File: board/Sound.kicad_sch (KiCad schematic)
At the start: 42 parts, among them J18 SJ1-3525N, J27 SND CT1/2, J39 LINE OUT, U57 YM2151, U58 YM3012, U59 TL074, U89 TDA2822M

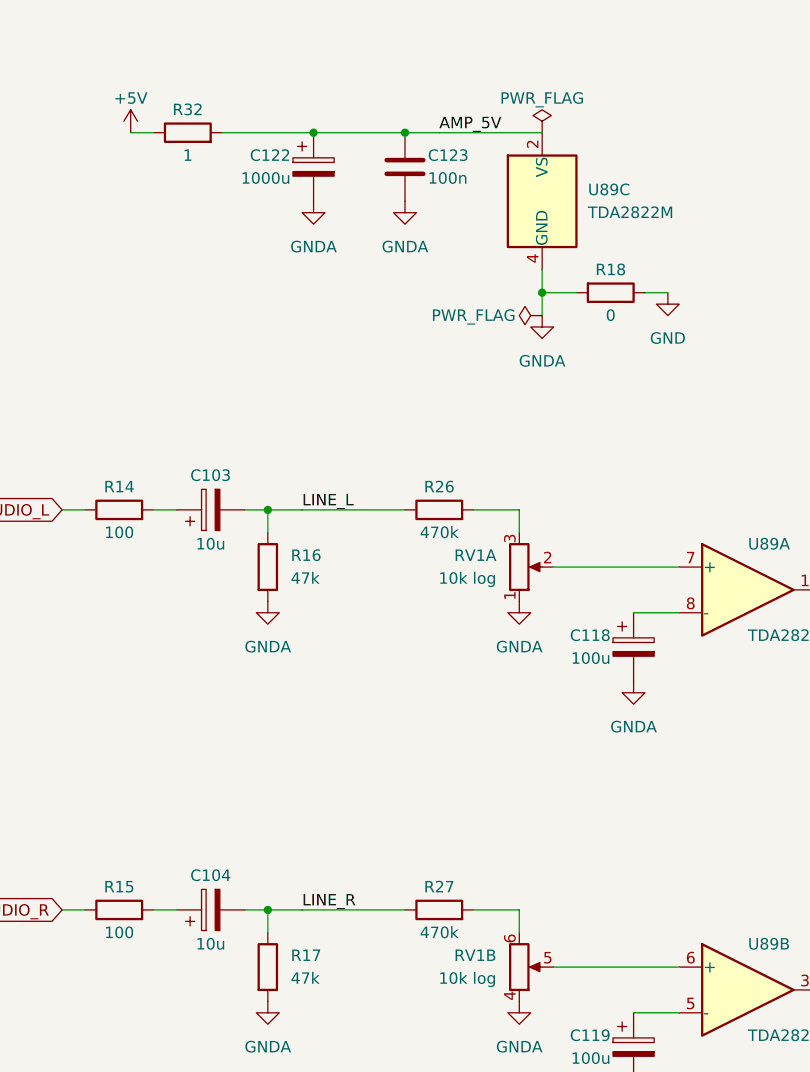
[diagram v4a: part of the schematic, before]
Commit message: V2.0: consolidate parts (239 -> 216), GAL C rev 02
No change in function:
- U9 74F08 removed: GAL C (U88) rev 02 makes the CPU phi0 (P_PHI0 = PHI2
  held low while DMAB_S is low); its decoupling cap C14 removed
- U34 74ACT14 removed: the two clock buffers use spare U19 74F240 gates
- U60 + U61 (2 x CY7C192 vector RAM) replaced by one AS7C256B-15
  (32K x 8, 15 ns); the IRQ sheet's D[0..7] bus is gone
- Crystal oscillators (U75 74HCU04, Y1, Y2, R1, R6-R8, C43, C44, C96,
  C97) replaced by canned oscillators X1 (14.31818 MHz), X2 (1.8432 MHz)
- Soft power: CD40106 -> 74HC14, CD4013 -> 74HC74 (active-low set/reset,
  power-on reset network inverted); a spare 74HC14 gate drives PS_ON#,
  so Q1 is removed
- R10-R13 -> RN6 (4 x 10k, SIP-5); R9, R21-R24 -> RN7 (5 x 33R isolated,
  SIP-10)
- C100-C102 (3 x 220u) -> C100 680u
- Clocks and Power sheet notes updated; PLD README updated

GAL C rev 02 verified against rev 01 over 200,000 clock edges.
PCB updated from the schematic (adds RN6, RN7, X1, X2 and the speakers
LS1/LS2). Also includes KiCad's re-save of the schematic sheets.

Co-Authored-By: Claude Opus 5.5 <noreply@anthropic.com>
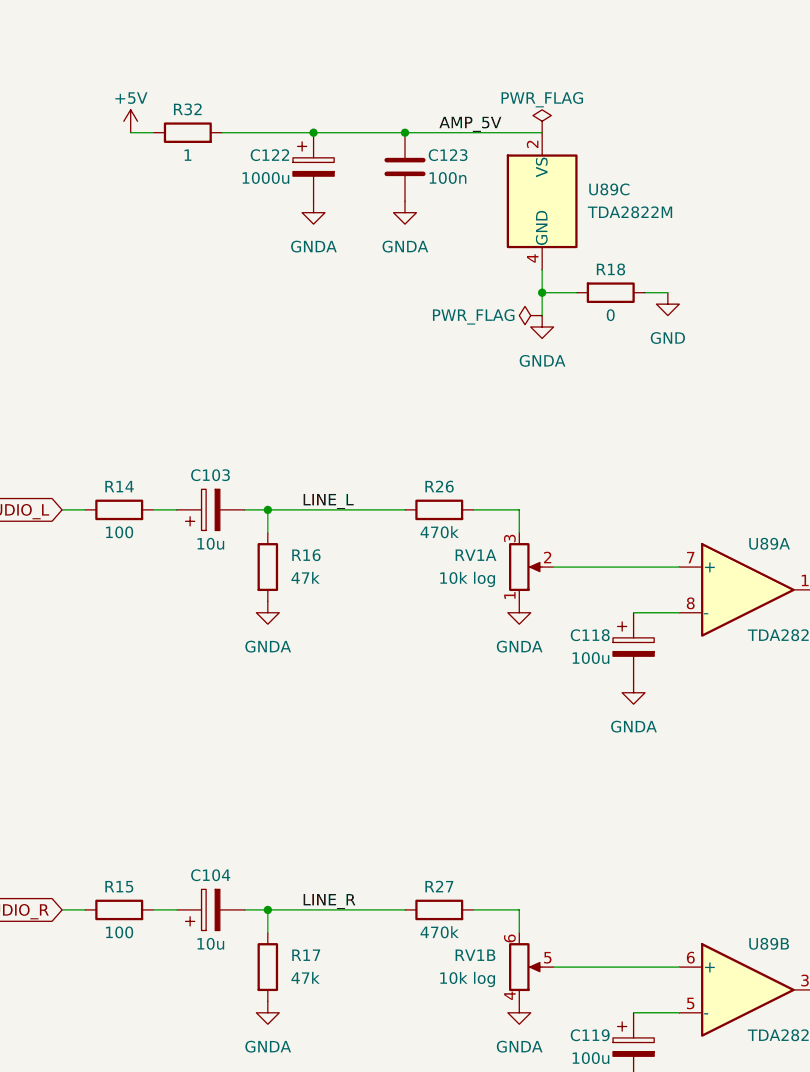
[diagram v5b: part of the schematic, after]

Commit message: V2.0: speaker headers, A/D bus fix, layout edits
- On-board speakers LS1/LS2 replaced by 2-pin headers J40 (SPEAKER L)
  and J41 (SPEAKER R) for external mini speakers: pin 1 speaker
  (through R30/R31), pin 2 GNDA; J18 still mutes them
- Connectors: a layout move had joined the A[0..15] and D[0..7] buses
  at two crossings (shorting A0-A7 to D0-D7); buses separated again,
  connectivity matches the previous commit
- Layout edits across the sheets (no other connectivity change)
- PCB updated from the schematic

Co-Authored-By: Claude Opus 5.5 <noreply@anthropic.com>
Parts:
- J40: renamed from LS1; value 8R mini -> SPEAKER L; footprint Hydra16:Speaker_D32mm_P15.24mm_P17.50mm -> Connector_PinHeader_2.54mm:PinHeader_1x02_P2.54mm_Vertical; symbol Device:Speaker -> Connector_Generic:Conn_01x02
- J41: renamed from LS2; value 8R mini -> SPEAKER R; footprint Hydra16:Speaker_D32mm_P15.24mm_P17.50mm -> Connector_PinHeader_2.54mm:PinHeader_1x02_P2.54mm_Vertical; symbol Device:Speaker -> Connector_Generic:Conn_01x02
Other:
- title: Sound: YM2151 / YM3012, Line Out, Amplifier and Speakers -> Expansion Slots, SPI Headers and Port A
- moved on the sheet: C103, C104, C105, C106, C107, C108, C109, C110, C116, C117, C118, C119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
